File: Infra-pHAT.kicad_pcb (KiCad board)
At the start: 2 copper layers, 64 x 30 mm, 24 parts, among them Q1 BC817, U1 CAT24C32WI-GT3

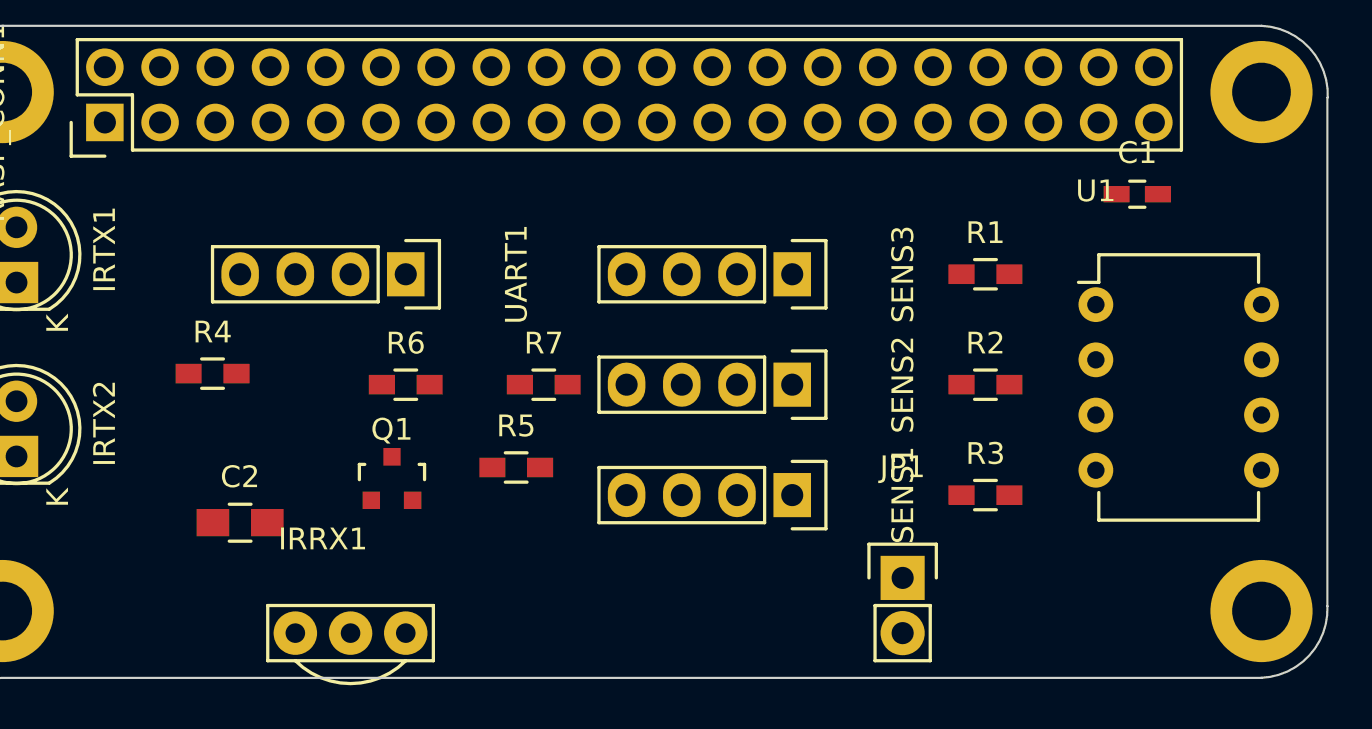
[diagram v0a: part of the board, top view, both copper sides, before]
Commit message: Infra-pHAT.kicad_pcb: Adjust positions
Signed-off-by: Leon Anavi <leon@anavi.org>
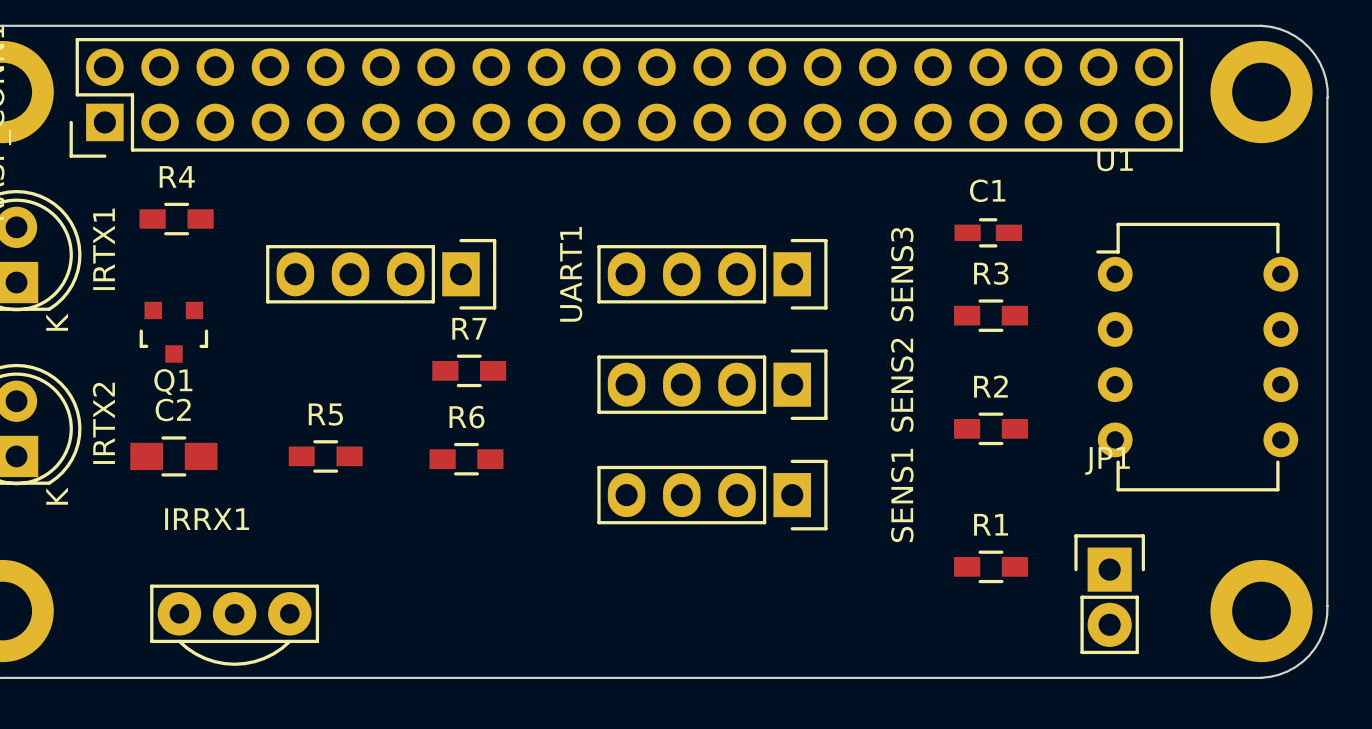
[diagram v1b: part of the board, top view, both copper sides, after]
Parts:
- moved R1 13.5 mm to (166.6, 120.1)
- moved Q1 12.1 mm to (129.0, 109.3), turned to 180 degrees
- moved JP1 9.53 mm to (172.1, 120.3)
- moved R5 8.78 mm to (136.0, 115.1)
- moved R3 8.26 mm to (166.6, 108.6)
- moved R4 7.30 mm to (129.2, 104.1)
- moved C1 7.08 mm to (166.5, 104.8)
- moved IRRX1 5.41 mm to (131.8, 119.8)
- moved R6 4.42 mm to (142.5, 115.2)
- moved C2 4.31 mm to (129.0, 115.1)
- moved R7 3.49 mm to (142.6, 111.1)
- moved UART1 2.54 mm to (142.2, 106.7)
- moved R2 2.05 mm to (166.6, 113.8)
- moved U1 1.66 mm to (172.3, 106.7)
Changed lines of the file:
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@@
     (34 B.Paste user)
     (35 F.Paste user)
-    (36 B.SilkS user)
+    (36 B.SilkS user hide)
     (37 F.SilkS user)
     (38 B.Mask user)
@@
     (40 Dwgs.User user)
     (41 Cmts.User user)
-    (42 Eco1.User user)
-    (43 Eco2.User user)
+    (42 Eco1.User user hide)
+    (43 Eco2.User user hide)
     (44 Edge.Cuts user)
     (45 Margin user)
     (46 B.CrtYd user)
     (47 F.CrtYd user)
-    (48 B.Fab user)
-    (49 F.Fab user)
+    (48 B.Fab user hide)
+    (49 F.Fab user hide)
   )
   (setup
@@
   )
   (module Capacitors_SMD:C_0603_HandSoldering (layer F.Cu)
-    (at 173.355 102.997)
+    (at 166.497 104.775)
     (descr "Capacitor SMD 0603, hand soldering")
     (tags "capacitor 0603")
@@
   )
   (module Capacitors_SMD:C_0805_HandSoldering (layer F.Cu)
-    (at 132.08 118.11)
+    (at 129.032 115.062)
     (descr "Capacitor SMD 0805, hand soldering")
     (tags "capacitor 0805")
@@
   )
   (module Pin_Headers:Pin_Header_Straight_1x02 (layer F.Cu)
-    (at 162.56 120.65)
+    (at 172.085 120.269)
     (descr "Through hole pin header")
     (tags "pin header")
@@
   )
   (module TO_SOT_Packages_SMD:SOT-23 (layer F.Cu)
-    (at 139.065 116.078)
+    (at 129.032 109.347 180)
     (descr "SOT-23, Standard")
     (tags SOT-23)
     (attr smd)
-    (fp_text reference Q1 (at 0 -2.25) (layer F.SilkS)
-      (effects (font (size 1 1) (thickness 0.15)))
-    )
-    (fp_text value BC817 (at 0 2.3) (layer F.Fab)
+    (fp_text reference Q1 (at 0 -2.25 180) (layer F.SilkS)
+      (effects (font (size 1 1) (thickness 0.15)))
+    )
+    (fp_text value BC817 (at 0 2.3 180) (layer F.Fab)
       (effects (font (size 1 1) (thickness 0.15)))
     )
@@
     (fp_line (start 1.29916 -0.65024) (end 1.49982 -0.65024) (layer F.SilkS) (width 0.15))
     (fp_line (start 1.49982 -0.65024) (end 1.49982 0.0508) (layer F.SilkS) (width 0.15))
-    (pad 1 smd rect (at -0.95 1.00076) (size 0.8001 0.8001) (layers F.Cu F.Paste F.Mask)
+    (pad 1 smd rect (at -0.95 1.00076 180) (size 0.8001 0.8001) (layers F.Cu F.Paste F.Mask)
       (net 7 "Net-(Q1-Pad1)"))
-    (pad 2 smd rect (at 0.95 1.00076) (size 0.8001 0.8001) (layers F.Cu F.Paste F.Mask))
-    (pad 3 smd rect (at 0 -0.99822) (size 0.8001 0.8001) (layers F.Cu F.Paste F.Mask)
+    (pad 2 smd rect (at 0.95 1.00076 180) (size 0.8001 0.8001) (layers F.Cu F.Paste F.Mask))
+    (pad 3 smd rect (at 0 -0.99822 180) (size 0.8001 0.8001) (layers F.Cu F.Paste F.Mask)
       (net 2 GND))
     (model TO_SOT_Packages_SMD.3dshapes/SOT-23.wrl
@@
   )
   (module Resistors_SMD:R_0603_HandSoldering (layer F.Cu)
-    (at 166.37 106.68)
+    (at 166.624 120.142)
     (descr "Resistor SMD 0603, hand soldering")
     (tags "resistor 0603")
@@
   )
   (module Resistors_SMD:R_0603_HandSoldering (layer F.Cu)
-    (at 166.37 111.76)
+    (at 166.624 113.792)
     (descr "Resistor SMD 0603, hand soldering")
     (tags "resistor 0603")
@@
   )
   (module Resistors_SMD:R_0603_HandSoldering (layer F.Cu)
-    (at 166.37 116.84)
+    (at 166.624 108.585)
     (descr "Resistor SMD 0603, hand soldering")
     (tags "resistor 0603")
@@
   )
   (module Resistors_SMD:R_0603_HandSoldering (layer F.Cu)
-    (at 130.81 111.252)
+    (at 129.159 104.14)
     (descr "Resistor SMD 0603, hand soldering")
     (tags "resistor 0603")
@@
   )
   (module Resistors_SMD:R_0603_HandSoldering (layer F.Cu)
-    (at 144.78 115.57)
+    (at 136.017 115.062)
     (descr "Resistor SMD 0603, hand soldering")
     (tags "resistor 0603")
@@
   )
   (module Resistors_SMD:R_0603_HandSoldering (layer F.Cu)
-    (at 139.7 111.76)
+    (at 142.494 115.189)
     (descr "Resistor SMD 0603, hand soldering")
     (tags "resistor 0603")
@@
   )
   (module Resistors_SMD:R_0603_HandSoldering (layer F.Cu)
-    (at 146.05 111.76)
+    (at 142.621 111.125)
     (descr "Resistor SMD 0603, hand soldering")
     (tags "resistor 0603")
@@
   )
   (module Housings_DIP:DIP-8_W7.62mm (layer F.Cu)
-    (at 171.45 108.077)
+    (at 172.339 106.68)
     (descr "8-lead dip package, row spacing 7.62 mm (300 mils)")
     (tags "dil dip 2.54 300")
@@
   )
   (module Pin_Headers:Pin_Header_Straight_1x04 (layer F.Cu)
-    (at 139.7 106.68 270)
+    (at 142.24 106.68 270)
     (descr "Through hole pin header")
     (tags "pin header")
@@
   )
   (module myfootprint:TSOP38X (layer F.Cu)
-    (at 137.16 120.65)
+    (at 131.826 119.761)
     (fp_text reference IRRX1 (at -1.27 -1.778) (layer F.SilkS)
       (effects (font (size 1 1) (thickness 0.15)))

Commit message: Infra-pHAT.kicad_pcb: Update settings
Increase traces and vias.

Signed-off-by: Leon Anavi <leon@anavi.org>
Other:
- net class Default: clearance 0.25 -> 0.254; trace_width 0.25 -> 0.5; via_dia 0.6 -> 0.85
- rule trace_clearance: 0.25 -> 0.254
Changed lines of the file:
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@@
     (links 59)
     (no_connects 59)
-    (area 118.046855 95.199999 182.17054 126.22)
+    (area 105.979429 93.923 194.248572 126.649)
     (thickness 1.6)
     (drawings 8)
@@
   )
   (setup
-    (last_trace_width 0.25)
-    (trace_clearance 0.25)
+    (last_trace_width 0.5)
+    (trace_clearance 0.254)
     (zone_clearance 0.508)
     (zone_45_only no)
@@
     (segment_width 0.2)
     (edge_width 0.1)
-    (via_size 0.6)
+    (via_size 0.85)
     (via_drill 0.4)
     (via_min_size 0.4)
     (via_min_drill 0.3)
-    (uvia_size 0.3)
+    (uvia_size 0.35)
     (uvia_drill 0.1)
     (uvias_allowed no)
@@
   (net 14 "Net-(IRRX1-Pad1)")
   (net_class Default "This is the default net class."
-    (clearance 0.25)
-    (trace_width 0.25)
-    (via_dia 0.6)
+    (clearance 0.254)
+    (trace_width 0.5)
+    (via_dia 0.85)
     (via_drill 0.4)
-    (uvia_dia 0.3)
+    (uvia_dia 0.35)
     (uvia_drill 0.1)
     (add_net +3V3)

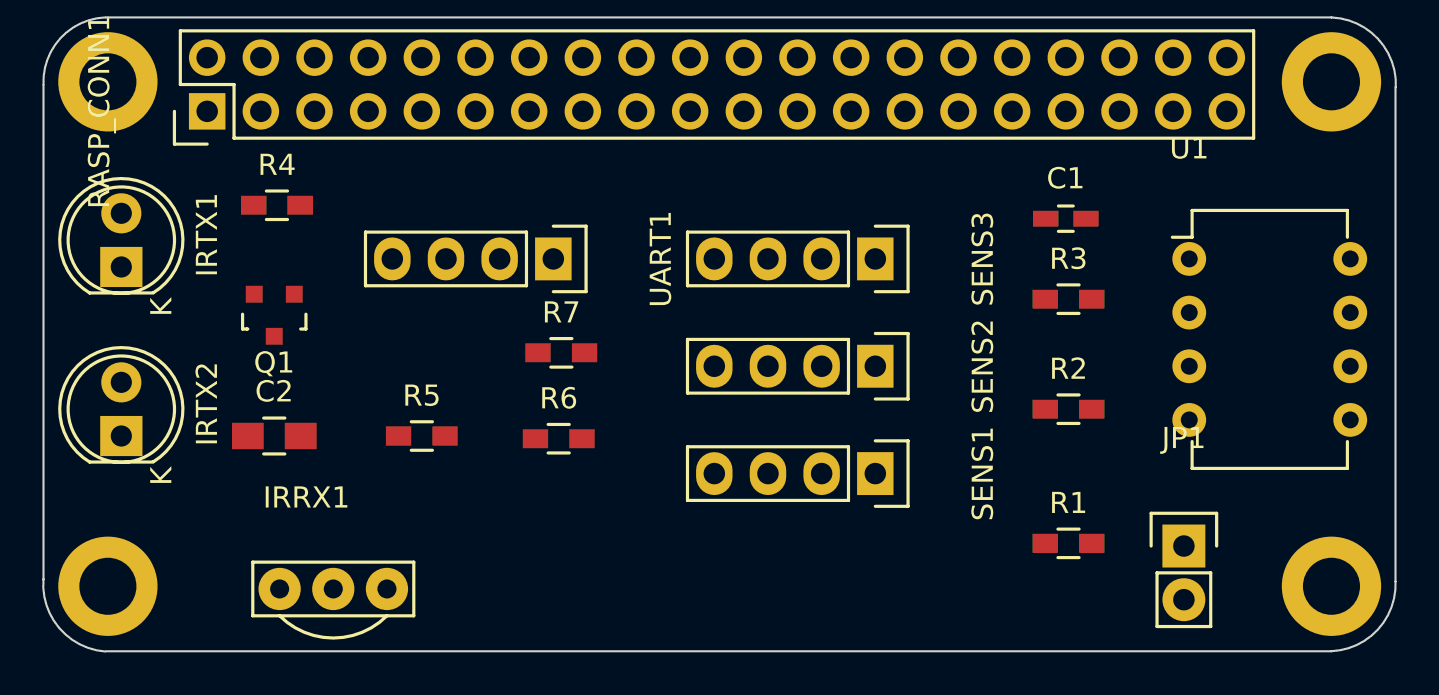
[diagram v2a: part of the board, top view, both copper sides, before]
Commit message: Infra-pHAT.kicad_pcb: Rearange components
Signed-off-by: Leon Anavi <leon@anavi.org>
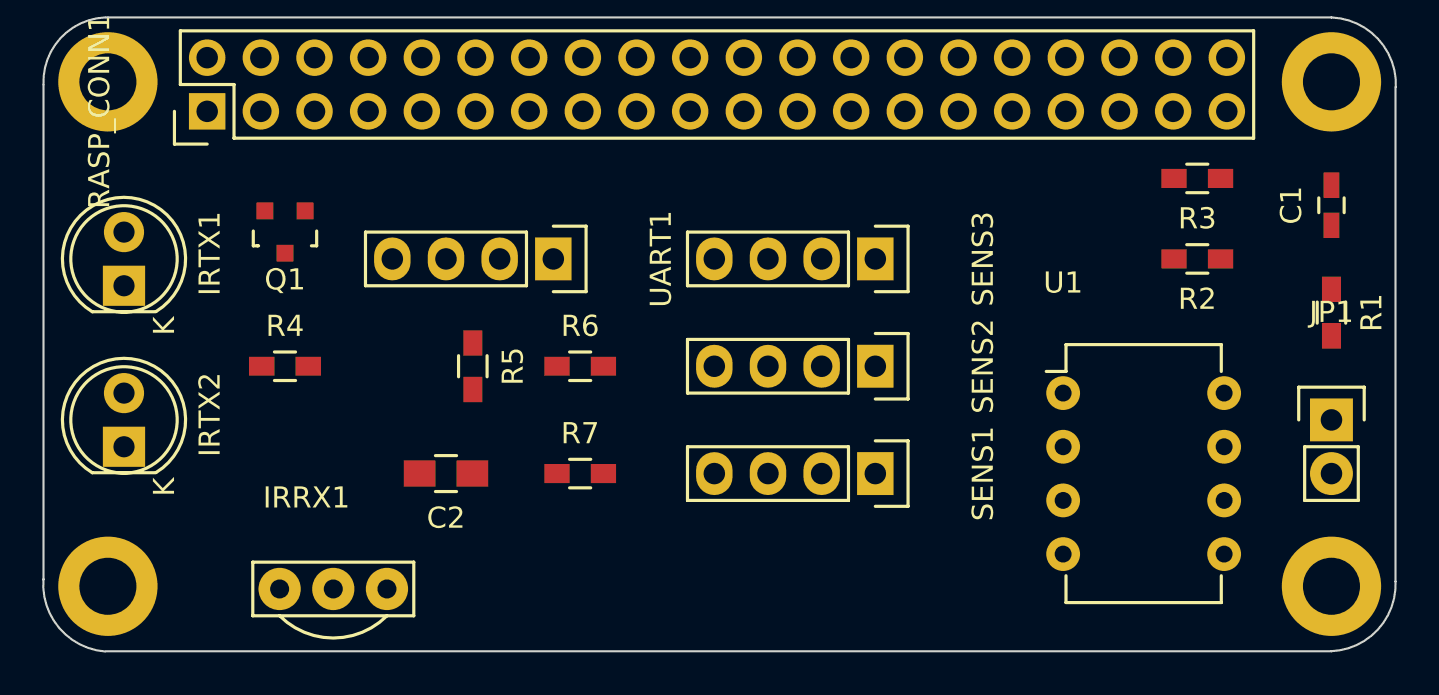
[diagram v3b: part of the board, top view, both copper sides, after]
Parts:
- moved R1 16.6 mm to (179.1, 109.2), turned to 270 degrees
- moved C1 12.6 mm to (179.1, 104.1), turned to 90 degrees
- moved R2 9.37 mm to (172.7, 106.7), turned to 180 degrees
- moved JP1 9.19 mm to (179.1, 114.3)
- moved U1 8.72 mm to (166.4, 113.0)
- moved R3 8.36 mm to (172.7, 102.9), turned to 180 degrees
- moved C2 8.32 mm to (137.2, 116.8), turned to 180 degrees
- moved R4 7.63 mm to (129.5, 111.8)
- moved R7 5.78 mm to (143.5, 116.8)
- moved R5 4.09 mm to (138.4, 111.8), turned to 270 degrees
- moved Q1 3.97 mm to (129.5, 105.4)
- moved R6 3.58 mm to (143.5, 111.8)
- moved IRTX1 0.90 mm to (121.9, 108.0)
- moved IRTX2 0.52 mm to (121.9, 115.6)
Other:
- net class vcc added: clearance 0.254, trace_width 1.5, via_dia 0.85, via_drill 0.4
